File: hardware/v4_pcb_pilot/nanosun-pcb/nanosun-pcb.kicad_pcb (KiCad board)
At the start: 2 copper layers, 29 parts, among them J1 Conn_01x03

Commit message: manually adjusted the pcb
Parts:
- removed C3: 470uF/25V, Capacitor_THT:CP_Radial_D8.0mm_P3.80mm
- C1, C2, J1, R1: moved to B.Cu
- moved LED14 160.4 mm to (225.0, 109.4), turned to 180 degrees
- moved LED12 159.5 mm to (225.0, 96.9), turned to 180 degrees
- moved LED10 158.6 mm to (225.0, 84.4), turned to 180 degrees
- moved LED18 154.0 mm to (218.8, 134.4), turned to 180 degrees
- moved LED16 153.4 mm to (218.8, 121.9), turned to 180 degrees
- moved LED8 142.2 mm to (218.8, 71.9), turned to 180 degrees
- moved LED20 131.2 mm to (206.2, 146.9), turned to 180 degrees
- moved LED6 127.0 mm to (212.5, 59.4), turned to 180 degrees
- moved J1 126.6 mm to (155.0, 23.5), turned to 180 degrees
- moved C2 110.3 mm to (151.8, 150.0), turned to 180 degrees
- moved LED22 107.1 mm to (193.8, 159.4), turned to 180 degrees
- moved LED4 104.0 mm to (200.0, 46.9), turned to 180 degrees
- moved LED2 85.7 mm to (187.5, 34.4), turned to 180 degrees
- moved C1 70.4 mm to (151.8, 50.0), turned to 180 degrees
- moved LED24 56.5 mm to (168.8, 171.9), turned to 180 degrees
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
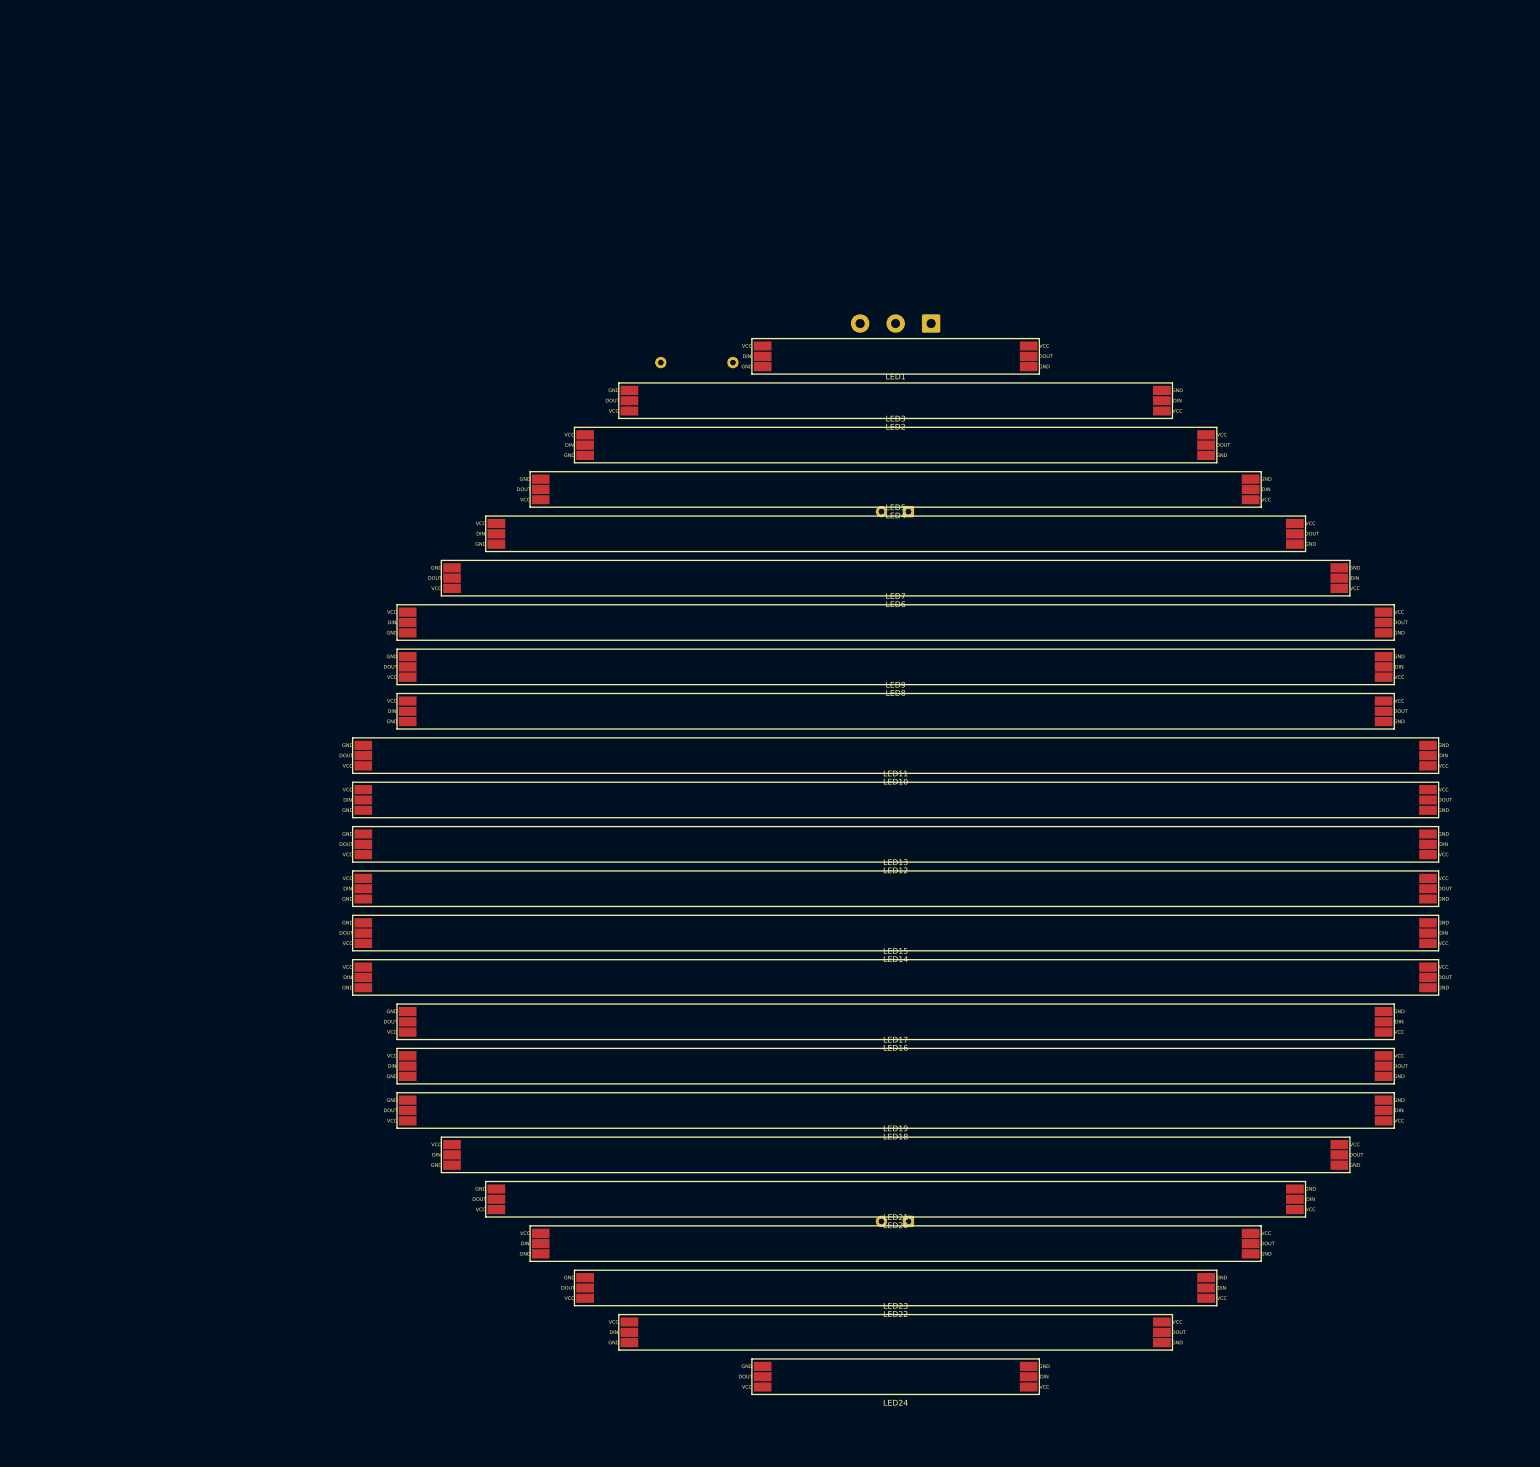
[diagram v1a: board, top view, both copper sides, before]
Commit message: circle pcb with touchups
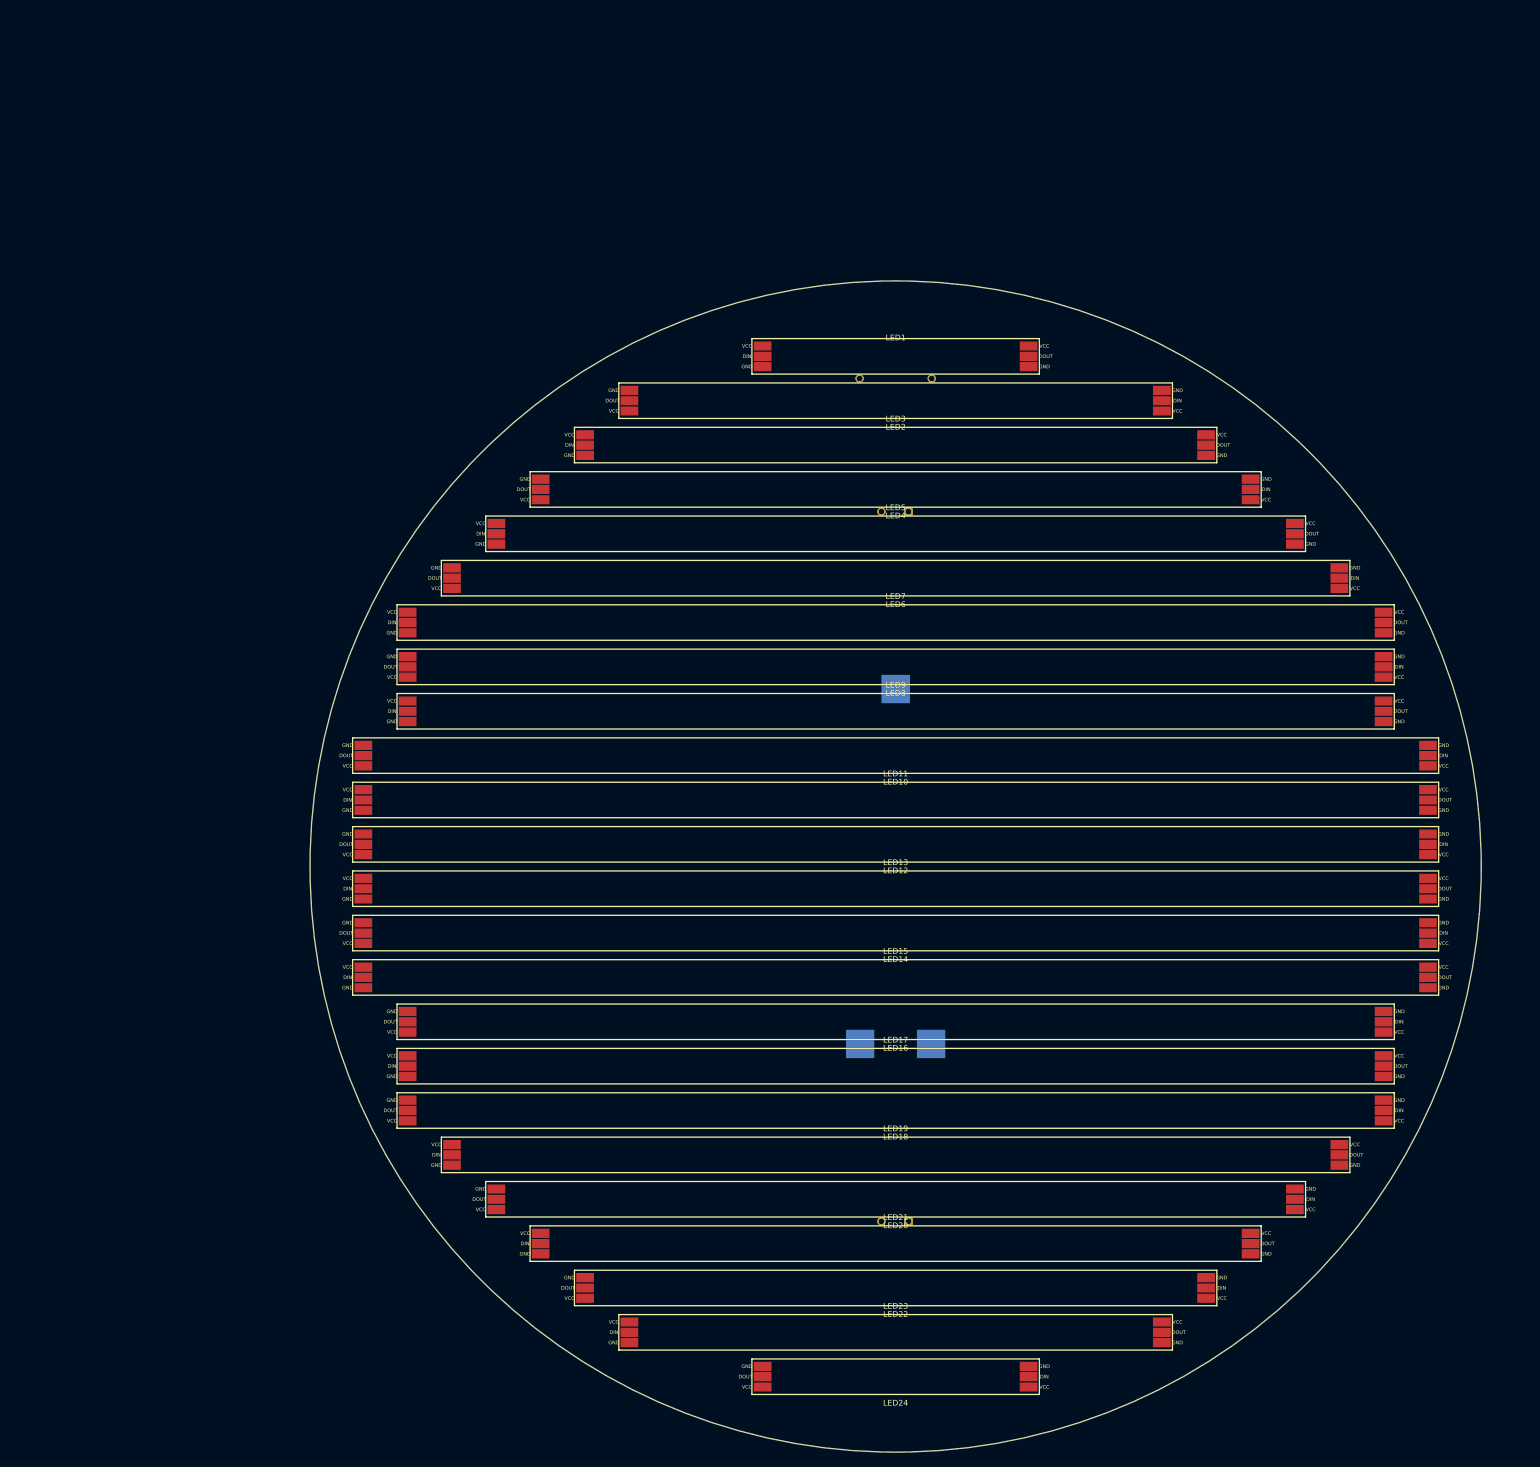
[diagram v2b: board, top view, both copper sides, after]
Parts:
- removed J1: Conn_01x03, TerminalBlock_Phoenix:TerminalBlock_Phoenix_MKDS-1,5-3_1x03_P5.00mm_Horizontal
- added 12V: +12V, nanosun-pcb:WireSolderPad_1, B.Cu at (155.0, 125.0)
- added DIN: DIN, nanosun-pcb:WireSolderPad_1, B.Cu at (150.0, 75.0)
- added GND: GND, nanosun-pcb:WireSolderPad_1, B.Cu at (145.0, 125.0)
- moved R1 28.1 mm to (155.1, 31.2)
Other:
- board outline added: 165 x 165 mm

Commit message: DRC fixes
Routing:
- net Net-(J2-Pad1): track 0.00 -> 44.0 mm
